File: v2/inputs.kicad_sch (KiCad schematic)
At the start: 7 parts, among them U5 74xx14

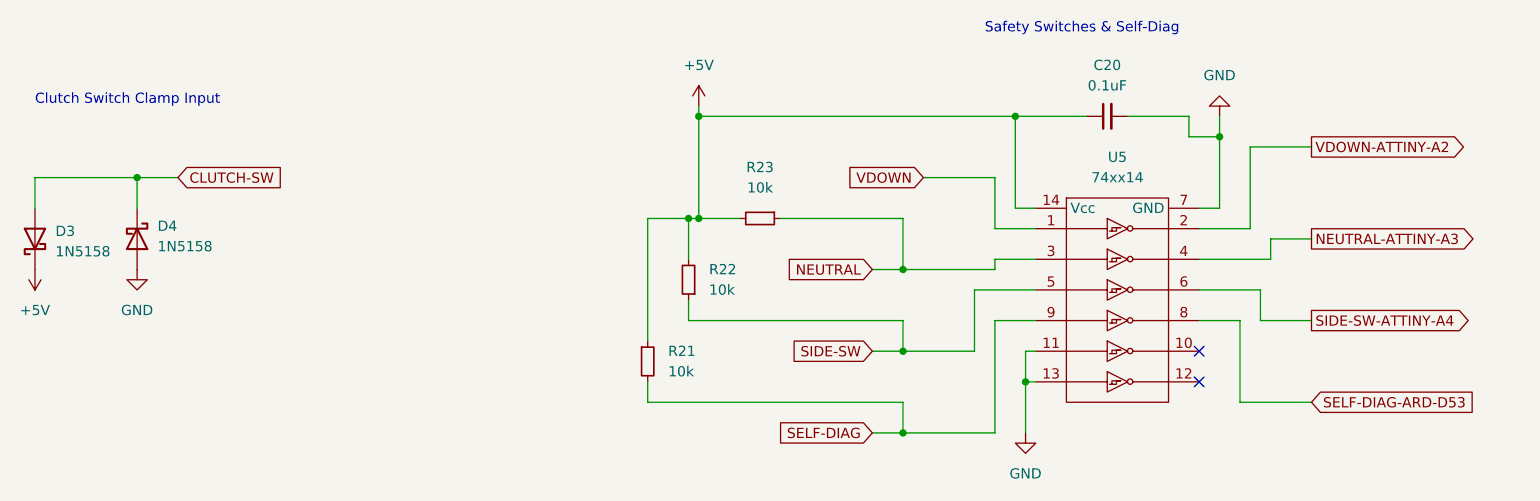
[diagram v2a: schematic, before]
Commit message: Delete ATTiny and associated circuitry
Control the secondary throttle w/ open loop stepper idle control in the speeduino firmware
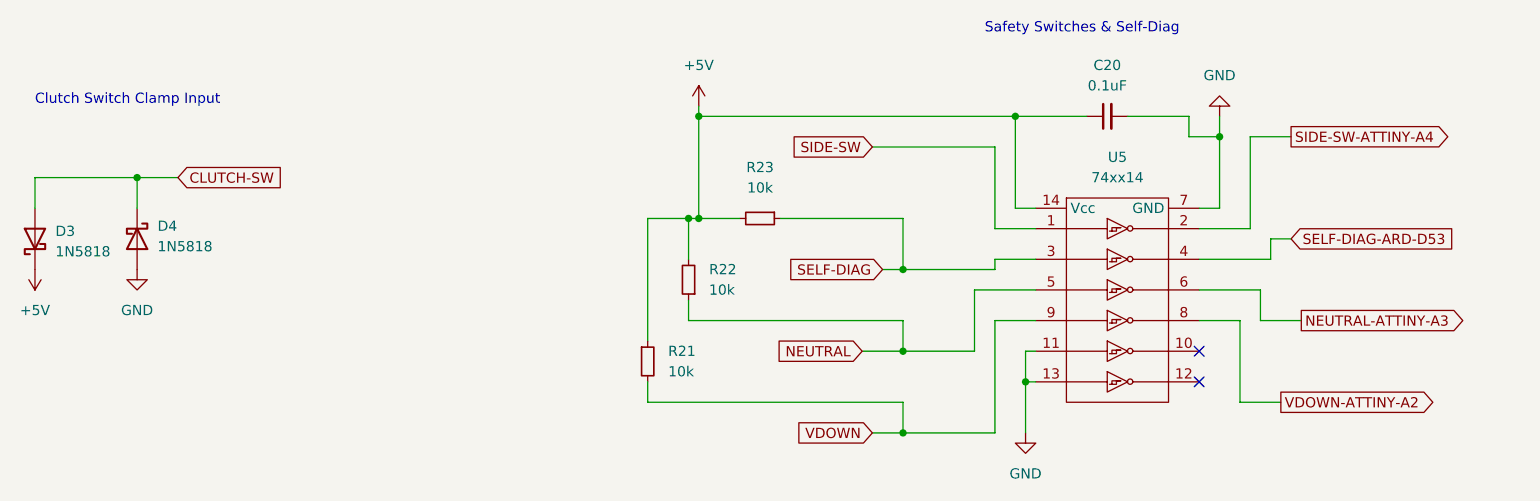
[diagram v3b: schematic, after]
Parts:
- D3, D4: value 1N5158 -> 1N5818
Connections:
- net NEUTRAL: now also R22.1, U5.5; no longer R23.1, U5.3
- net NEUTRAL-ATTINY-A3: now also U5.6; no longer U5.4
- net SELF-DIAG: now also R23.1, U5.3; no longer R21.2, U5.9
- net SELF-DIAG-ARD-D53: now also U5.4; no longer U5.8
- net SIDE-SW: now also U5.1; no longer R22.1, U5.5
- net SIDE-SW-ATTINY-A4: now also U5.2; no longer U5.6
- net VDOWN: now also R21.2, U5.9; no longer U5.1
- net VDOWN-ATTINY-A2: now also U5.8; no longer U5.2
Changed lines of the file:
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@@
   (junction (at 185.42 36.83) (diameter 0) (color 0 0 0 0)
   )
+  (junction (at 120.65 34.29) (diameter 0) (color 0 0 0 0)
+  )
+  (junction (at 146.05 53.34) (diameter 0) (color 0 0 0 0)
+  )
+  (junction (at 120.65 46.99) (diameter 0) (color 0 0 0 0)
+  )
+  (junction (at 146.05 73.66) (diameter 0) (color 0 0 0 0)
+  )
+  (junction (at 119.38 46.99) (diameter 0) (color 0 0 0 0)
+  )
   (junction (at 146.05 63.5) (diameter 0) (color 0 0 0 0)
-  )
-  (junction (at 146.05 73.66) (diameter 0) (color 0 0 0 0)
-  )
-  (junction (at 120.65 34.29) (diameter 0) (color 0 0 0 0)
-  )
-  (junction (at 120.65 46.99) (diameter 0) (color 0 0 0 0)
-  )
-  (junction (at 119.38 46.99) (diameter 0) (color 0 0 0 0)
-  )
-  (junction (at 146.05 53.34) (diameter 0) (color 0 0 0 0)
   )
   (no_connect (at 182.88 63.5))
@@
     (stroke (width 0) (type default) (color 0 0 0 0))
   )
+  (wire (pts (xy 142.24 38.1) (xy 157.48 38.1))
+    (stroke (width 0) (type default) (color 0 0 0 0))
+  )
   (wire (pts (xy 119.38 57.15) (xy 119.38 59.69))
     (stroke (width 0) (type default) (color 0 0 0 0))
@@
     (stroke (width 0) (type default) (color 0 0 0 0))
   )
+  (wire (pts (xy 190.5 59.69) (xy 195.58 59.69))
+    (stroke (width 0) (type default) (color 0 0 0 0))
+  )
   (wire (pts (xy 182.88 52.07) (xy 191.77 52.07))
     (stroke (width 0) (type default) (color 0 0 0 0))
   )
+  (wire (pts (xy 157.48 38.1) (xy 157.48 48.26))
+    (stroke (width 0) (type default) (color 0 0 0 0))
+  )
   (wire (pts (xy 160.02 34.29) (xy 160.02 45.72))
     (stroke (width 0) (type default) (color 0 0 0 0))
@@
     (stroke (width 0) (type default) (color 0 0 0 0))
   )
-  (wire (pts (xy 148.59 41.91) (xy 157.48 41.91))
-    (stroke (width 0) (type default) (color 0 0 0 0))
-  )
-  (wire (pts (xy 142.24 63.5) (xy 146.05 63.5))
-    (stroke (width 0) (type default) (color 0 0 0 0))
-  )
   (wire (pts (xy 38.1 41.91) (xy 50.8 41.91))
     (stroke (width 0) (type default) (color 0 0 0 0))
@@
     (stroke (width 0) (type default) (color 0 0 0 0))
   )
-  (wire (pts (xy 187.96 69.85) (xy 196.85 69.85))
-    (stroke (width 0) (type default) (color 0 0 0 0))
-  )
   (wire (pts (xy 120.65 33.02) (xy 120.65 34.29))
     (stroke (width 0) (type default) (color 0 0 0 0))
   )
+  (wire (pts (xy 187.96 69.85) (xy 193.04 69.85))
+    (stroke (width 0) (type default) (color 0 0 0 0))
+  )
+  (wire (pts (xy 142.24 73.66) (xy 146.05 73.66))
+    (stroke (width 0) (type default) (color 0 0 0 0))
+  )
   (wire (pts (xy 114.3 46.99) (xy 114.3 62.23))
     (stroke (width 0) (type default) (color 0 0 0 0))
@@
     (stroke (width 0) (type default) (color 0 0 0 0))
   )
-  (wire (pts (xy 142.24 53.34) (xy 146.05 53.34))
-    (stroke (width 0) (type default) (color 0 0 0 0))
-  )
   (wire (pts (xy 154.94 63.5) (xy 154.94 55.88))
     (stroke (width 0) (type default) (color 0 0 0 0))
@@
     (stroke (width 0) (type default) (color 0 0 0 0))
   )
+  (wire (pts (xy 143.51 53.34) (xy 146.05 53.34))
+    (stroke (width 0) (type default) (color 0 0 0 0))
+  )
   (wire (pts (xy 146.05 59.69) (xy 146.05 63.5))
     (stroke (width 0) (type default) (color 0 0 0 0))
   )
-  (wire (pts (xy 157.48 41.91) (xy 157.48 48.26))
-    (stroke (width 0) (type default) (color 0 0 0 0))
-  )
   (wire (pts (xy 185.42 34.29) (xy 185.42 36.83))
     (stroke (width 0) (type default) (color 0 0 0 0))
@@
     (stroke (width 0) (type default) (color 0 0 0 0))
   )
-  (wire (pts (xy 190.5 59.69) (xy 196.85 59.69))
+  (wire (pts (xy 140.97 63.5) (xy 146.05 63.5))
     (stroke (width 0) (type default) (color 0 0 0 0))
   )
@@
     (stroke (width 0) (type default) (color 0 0 0 0))
   )
-  (wire (pts (xy 189.23 38.1) (xy 196.85 38.1))
-    (stroke (width 0) (type default) (color 0 0 0 0))
-  )
   (wire (pts (xy 120.65 46.99) (xy 119.38 46.99))
     (stroke (width 0) (type default) (color 0 0 0 0))
@@
     (stroke (width 0) (type default) (color 0 0 0 0))
   )
-  (wire (pts (xy 189.23 48.26) (xy 189.23 38.1))
+  (wire (pts (xy 189.23 36.83) (xy 194.31 36.83))
+    (stroke (width 0) (type default) (color 0 0 0 0))
+  )
+  (wire (pts (xy 189.23 36.83) (xy 189.23 48.26))
     (stroke (width 0) (type default) (color 0 0 0 0))
   )
@@
     (stroke (width 0) (type default) (color 0 0 0 0))
   )
-  (wire (pts (xy 142.24 73.66) (xy 146.05 73.66))
-    (stroke (width 0) (type default) (color 0 0 0 0))
-  )
   (wire (pts (xy 160.02 45.72) (xy 162.56 45.72))
     (stroke (width 0) (type default) (color 0 0 0 0))
   )
-  (wire (pts (xy 191.77 49.53) (xy 196.85 49.53))
-    (stroke (width 0) (type default) (color 0 0 0 0))
-  )
   (wire (pts (xy 146.05 46.99) (xy 146.05 53.34))
+    (stroke (width 0) (type default) (color 0 0 0 0))
+  )
+  (wire (pts (xy 191.77 49.53) (xy 194.31 49.53))
     (stroke (width 0) (type default) (color 0 0 0 0))
   )
@@
     (effects (font (size 1.27 1.27)) (justify left bottom))
   )
-  (global_label "SIDE-SW" (shape input) (at 142.24 63.5 180) (fields_autoplaced)
+  (global_label "SIDE-SW" (shape input) (at 142.24 38.1 180) (fields_autoplaced)
     (effects (font (size 1.27 1.27)) (justify right))
-    (property "Intersheet References" "${INTERSHEET_REFS}" (id 0) (at 131.3602 63.4206 0)
+    (property "Intersheet References" "${INTERSHEET_REFS}" (id 0) (at 131.3602 38.0206 0)
       (effects (font (size 1.27 1.27)) (justify right) hide)
     )
@@
     )
   )
-  (global_label "VDOWN-ATTINY-A2" (shape output) (at 196.85 38.1 0) (fields_autoplaced)
+  (global_label "VDOWN-ATTINY-A2" (shape output) (at 193.04 69.85 0) (fields_autoplaced)
     (effects (font (size 1.27 1.27)) (justify left))
-    (property "Intersheet References" "${INTERSHEET_REFS}" (id 0) (at 217.2245 38.0206 0)
+    (property "Intersheet References" "${INTERSHEET_REFS}" (id 0) (at 213.4145 69.7706 0)
       (effects (font (size 1.27 1.27)) (justify left) hide)
     )
   )
-  (global_label "NEUTRAL" (shape input) (at 142.24 53.34 180) (fields_autoplaced)
+  (global_label "NEUTRAL" (shape input) (at 140.97 63.5 180) (fields_autoplaced)
     (effects (font (size 1.27 1.27)) (justify right))
-    (property "Intersheet References" "${INTERSHEET_REFS}" (id 0) (at 131.6626 53.2606 0)
+    (property "Intersheet References" "${INTERSHEET_REFS}" (id 0) (at 130.3926 63.4206 0)
       (effects (font (size 1.27 1.27)) (justify right) hide)
     )
   )
-  (global_label "VDOWN" (shape input) (at 148.59 41.91 180) (fields_autoplaced)
+  (global_label "VDOWN" (shape input) (at 142.24 73.66 180) (fields_autoplaced)
     (effects (font (size 1.27 1.27)) (justify right))
-    (property "Intersheet References" "${INTERSHEET_REFS}" (id 0) (at 139.7059 41.8306 0)
+    (property "Intersheet References" "${INTERSHEET_REFS}" (id 0) (at 133.3559 73.5806 0)
       (effects (font (size 1.27 1.27)) (justify right) hide)
     )
   )
-  (global_label "SELF-DIAG" (shape input) (at 142.24 73.66 180) (fields_autoplaced)
+  (global_label "SELF-DIAG" (shape input) (at 143.51 53.34 180) (fields_autoplaced)
     (effects (font (size 1.27 1.27)) (justify right))
-    (property "Intersheet References" "${INTERSHEET_REFS}" (id 0) (at 129.5459 73.5806 0)
+    (property "Intersheet References" "${INTERSHEET_REFS}" (id 0) (at 130.8159 53.2606 0)
       (effects (font (size 1.27 1.27)) (justify right) hide)
     )
   )
-  (global_label "SIDE-SW-ATTINY-A4" (shape output) (at 196.85 59.69 0) (fields_autoplaced)
+  (global_label "SIDE-SW-ATTINY-A4" (shape output) (at 194.31 36.83 0) (fields_autoplaced)
     (effects (font (size 1.27 1.27)) (justify left))
-    (property "Intersheet References" "${INTERSHEET_REFS}" (id 0) (at 219.2202 59.6106 0)
+    (property "Intersheet References" "${INTERSHEET_REFS}" (id 0) (at 216.6802 36.7506 0)
       (effects (font (size 1.27 1.27)) (justify left) hide)
     )
   )
-  (global_label "SELF-DIAG-ARD-D53" (shape input) (at 196.85 69.85 0) (fields_autoplaced)
+  (global_label "SELF-DIAG-ARD-D53" (shape input) (at 194.31 49.53 0) (fields_autoplaced)
     (effects (font (size 1.27 1.27)) (justify left))
-    (property "Intersheet References" "${INTERSHEET_REFS}" (id 0) (at 220.0064 69.7706 0)
+    (property "Intersheet References" "${INTERSHEET_REFS}" (id 0) (at 217.4664 49.4506 0)
       (effects (font (size 1.27 1.27)) (justify left) hide)
     )
   )
-  (global_label "NEUTRAL-ATTINY-A3" (shape output) (at 196.85 49.53 0) (fields_autoplaced)
+  (global_label "NEUTRAL-ATTINY-A3" (shape output) (at 195.58 59.69 0) (fields_autoplaced)
     (effects (font (size 1.27 1.27)) (justify left))
-    (property "Intersheet References" "${INTERSHEET_REFS}" (id 0) (at 218.9179 49.4506 0)
+    (property "Intersheet References" "${INTERSHEET_REFS}" (id 0) (at 217.6479 59.6106 0)
       (effects (font (size 1.27 1.27)) (justify left) hide)
     )
@@
       (effects (font (size 1.27 1.27)) (justify right))
     )
-    (property "Value" "1N5158" (id 1) (at 40.64 51.1174 90)
+    (property "Value" "1N5818" (id 1) (at 40.64 51.1174 90)
       (effects (font (size 1.27 1.27)) (justify right))
     )
@@
       (effects (font (size 1.27 1.27)) (justify left))
     )
-    (property "Value" "1N5158" (id 1) (at 53.34 50.4824 90)
+    (property "Value" "1N5818" (id 1) (at 53.34 50.4824 90)
       (effects (font (size 1.27 1.27)) (justify left))
     )
